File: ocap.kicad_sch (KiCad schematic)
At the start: 7 parts

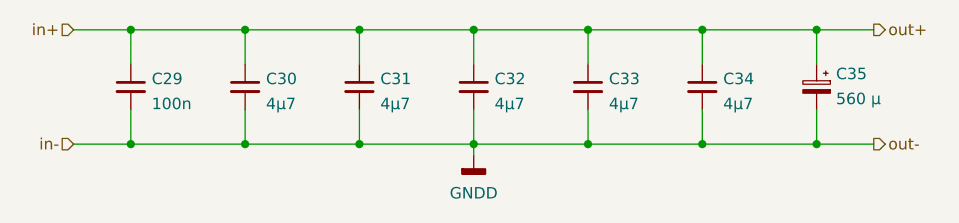
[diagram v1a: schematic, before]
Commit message: Clean up schematic
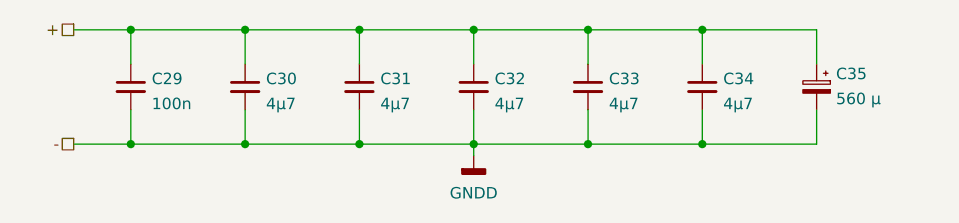
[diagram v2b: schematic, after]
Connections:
- net in+ renamed +

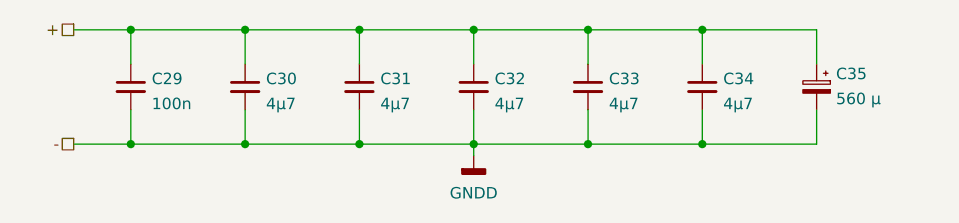
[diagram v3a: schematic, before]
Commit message: Add separate ADCs for remote measurements
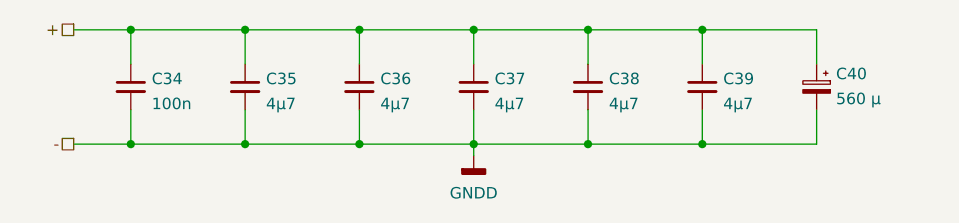
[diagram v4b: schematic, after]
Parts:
- C34: renamed from C29; Part Number GRM155R71H102KA01J -> GRM155R71H104KE14D
- renumbered C30 to C35, C31 to C36, C32 to C37, C33 to C38, C34 to C39, C35 to C40
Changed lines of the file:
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@@
   (symbol (lib_id "Device:C_Small") (at 114.3 95.25 0) (unit 1)
     (in_bom yes) (on_board yes) (fields_autoplaced)
-    (property "Reference" "C29" (id 0) (at 116.6241 94.3478 0)
+    (property "Reference" "C34" (id 0) (at 116.6241 94.3478 0)
       (effects (font (size 1.27 1.27)) (justify left))
     )
@@
       (effects (font (size 1.27 1.27)) hide)
     )
-    (property "Part Number" "GRM155R71H102KA01J" (id 5) (at 114.3 95.25 0)
+    (property "Part Number" " GRM155R71H104KE14D" (id 5) (at 114.3 95.25 0)
       (effects (font (size 1.27 1.27)) hide)
     )
@@
   (symbol (lib_id "Device:C_Small") (at 139.7 95.25 0) (unit 1)
     (in_bom yes) (on_board yes) (fields_autoplaced)
-    (property "Reference" "C31" (id 0) (at 142.0241 94.3478 0)
+    (property "Reference" "C36" (id 0) (at 142.0241 94.3478 0)
       (effects (font (size 1.27 1.27)) (justify left))
     )
@@
   (symbol (lib_id "Device:C_Polarized_Small") (at 190.5 95.25 0) (mirror y) (unit 1)
     (in_bom yes) (on_board yes) (fields_autoplaced)
-    (property "Reference" "C35" (id 0) (at 192.659 93.7954 0)
+    (property "Reference" "C40" (id 0) (at 192.659 93.7954 0)
       (effects (font (size 1.27 1.27)) (justify right))
     )
@@
   (symbol (lib_id "Device:C_Small") (at 127 95.25 0) (unit 1)
     (in_bom yes) (on_board yes) (fields_autoplaced)
-    (property "Reference" "C30" (id 0) (at 129.3241 94.3478 0)
+    (property "Reference" "C35" (id 0) (at 129.3241 94.3478 0)
       (effects (font (size 1.27 1.27)) (justify left))
     )
@@
   (symbol (lib_id "Device:C_Small") (at 165.1 95.25 0) (unit 1)
     (in_bom yes) (on_board yes) (fields_autoplaced)
-    (property "Reference" "C33" (id 0) (at 167.4241 94.3478 0)
+    (property "Reference" "C38" (id 0) (at 167.4241 94.3478 0)
       (effects (font (size 1.27 1.27)) (justify left))
     )
@@
   (symbol (lib_id "Device:C_Small") (at 152.4 95.25 0) (unit 1)
     (in_bom yes) (on_board yes) (fields_autoplaced)
-    (property "Reference" "C32" (id 0) (at 154.7241 94.3478 0)
+    (property "Reference" "C37" (id 0) (at 154.7241 94.3478 0)
       (effects (font (size 1.27 1.27)) (justify left))
     )
@@
   (symbol (lib_id "Device:C_Small") (at 177.8 95.25 0) (unit 1)
     (in_bom yes) (on_board yes) (fields_autoplaced)
-    (property "Reference" "C34" (id 0) (at 180.1241 94.3478 0)
+    (property "Reference" "C39" (id 0) (at 180.1241 94.3478 0)
       (effects (font (size 1.27 1.27)) (justify left))
     )
@@
   (symbol (lib_id "power:GNDD") (at 152.4 102.87 0) (unit 1)
     (in_bom yes) (on_board yes) (fields_autoplaced)
-    (property "Reference" "#PWR067" (id 0) (at 152.4 109.22 0)
+    (property "Reference" "#PWR091" (id 0) (at 152.4 109.22 0)
       (effects (font (size 1.27 1.27)) hide)
     )

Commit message: Add 100 nF bypass capacitor to ESP32 power input
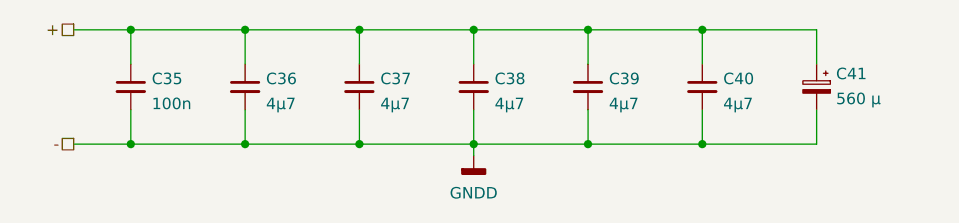
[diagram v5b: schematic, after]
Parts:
- renumbered C34 to C35, C35 to C36, C36 to C37, C37 to C38, C38 to C39, C39 to C40, C40 to C41
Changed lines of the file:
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@@
   (symbol (lib_id "Device:C_Small") (at 114.3 95.25 0) (unit 1)
     (in_bom yes) (on_board yes) (fields_autoplaced)
-    (property "Reference" "C34" (id 0) (at 116.6241 94.3478 0)
+    (property "Reference" "C35" (id 0) (at 116.6241 94.3478 0)
       (effects (font (size 1.27 1.27)) (justify left))
     )
@@
   (symbol (lib_id "Device:C_Small") (at 139.7 95.25 0) (unit 1)
     (in_bom yes) (on_board yes) (fields_autoplaced)
-    (property "Reference" "C36" (id 0) (at 142.0241 94.3478 0)
+    (property "Reference" "C37" (id 0) (at 142.0241 94.3478 0)
       (effects (font (size 1.27 1.27)) (justify left))
     )
@@
   (symbol (lib_id "Device:C_Polarized_Small") (at 190.5 95.25 0) (mirror y) (unit 1)
     (in_bom yes) (on_board yes) (fields_autoplaced)
-    (property "Reference" "C40" (id 0) (at 192.659 93.7954 0)
+    (property "Reference" "C41" (id 0) (at 192.659 93.7954 0)
       (effects (font (size 1.27 1.27)) (justify right))
     )
@@
   (symbol (lib_id "Device:C_Small") (at 127 95.25 0) (unit 1)
     (in_bom yes) (on_board yes) (fields_autoplaced)
-    (property "Reference" "C35" (id 0) (at 129.3241 94.3478 0)
+    (property "Reference" "C36" (id 0) (at 129.3241 94.3478 0)
       (effects (font (size 1.27 1.27)) (justify left))
     )
@@
   (symbol (lib_id "Device:C_Small") (at 165.1 95.25 0) (unit 1)
     (in_bom yes) (on_board yes) (fields_autoplaced)
-    (property "Reference" "C38" (id 0) (at 167.4241 94.3478 0)
+    (property "Reference" "C39" (id 0) (at 167.4241 94.3478 0)
       (effects (font (size 1.27 1.27)) (justify left))
     )
@@
   (symbol (lib_id "Device:C_Small") (at 152.4 95.25 0) (unit 1)
     (in_bom yes) (on_board yes) (fields_autoplaced)
-    (property "Reference" "C37" (id 0) (at 154.7241 94.3478 0)
+    (property "Reference" "C38" (id 0) (at 154.7241 94.3478 0)
       (effects (font (size 1.27 1.27)) (justify left))
     )
@@
   (symbol (lib_id "Device:C_Small") (at 177.8 95.25 0) (unit 1)
     (in_bom yes) (on_board yes) (fields_autoplaced)
-    (property "Reference" "C39" (id 0) (at 180.1241 94.3478 0)
+    (property "Reference" "C40" (id 0) (at 180.1241 94.3478 0)
       (effects (font (size 1.27 1.27)) (justify left))
     )
@@
   (symbol (lib_id "power:GNDD") (at 152.4 102.87 0) (unit 1)
     (in_bom yes) (on_board yes) (fields_autoplaced)
-    (property "Reference" "#PWR091" (id 0) (at 152.4 109.22 0)
+    (property "Reference" "#PWR092" (id 0) (at 152.4 109.22 0)
       (effects (font (size 1.27 1.27)) hide)
     )
